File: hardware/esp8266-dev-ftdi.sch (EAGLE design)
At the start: 53 parts, among them CON1 USBMICRO-NO_CENTER-LONG_PADS

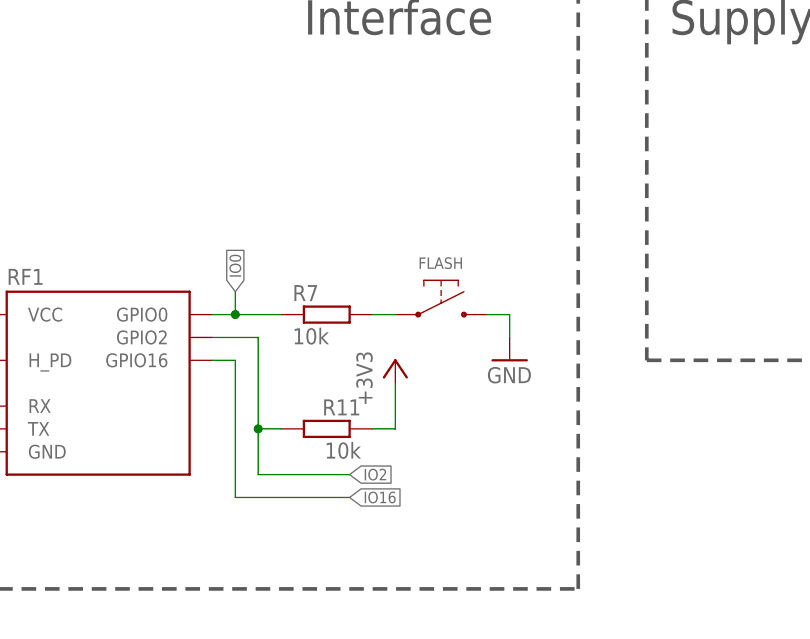
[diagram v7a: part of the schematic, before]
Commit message: added led to gpio2
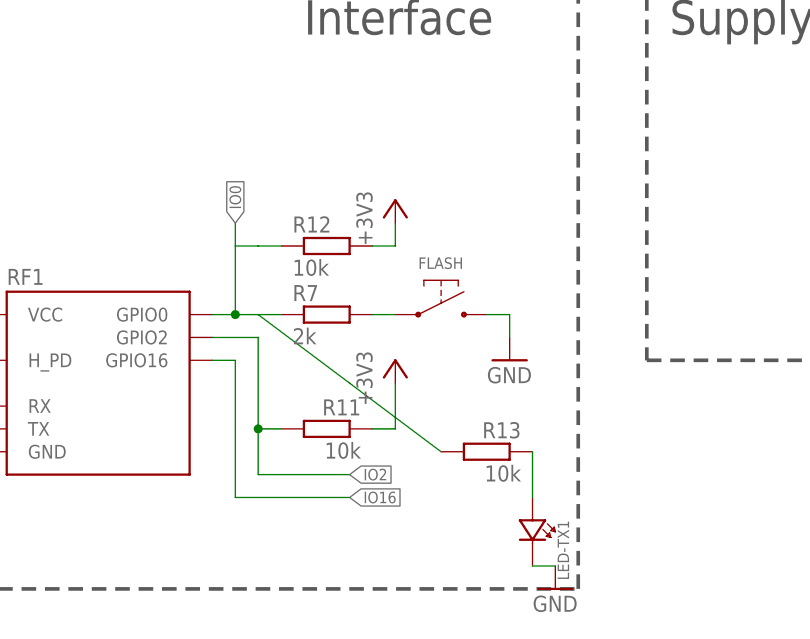
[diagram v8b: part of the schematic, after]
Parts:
- added LED-TX1: (no value), p.peter-leds:LED0805
- added R12, R13: 10k, p.peter-rcl:R-EU_R0805
- R7: value 10k -> 2k
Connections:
- new net N$22: LED-TX1.A, R13.1
- net +3V3: now also R12.2
- net GND: now also LED-TX1.C
- net IO0: now also R12.1, R13.2
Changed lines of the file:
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@@
 <?xml version="1.0" encoding="utf-8"?>
 <!DOCTYPE eagle SYSTEM "eagle.dtd">
-<eagle version="7.3.0">
+<eagle version="7.1.0">
 <drawing>
 <settings>
@@
 <part name="R6" library="p.peter-rcl" deviceset="R-EU_" device="R0805" value="10k"/>
 <part name="+3V8" library="supply1" deviceset="+3V3" device=""/>
-<part name="R7" library="p.peter-rcl" deviceset="R-EU_" device="R0805" value="10k"/>
+<part name="R7" library="p.peter-rcl" deviceset="R-EU_" device="R0805" value="2k"/>
 <part name="GND13" library="supply1" deviceset="GND" device=""/>
 <part name="U$2" library="p.peter-connectors" deviceset="UART-6_PIN" device="GENERIC"/>
@@
 <part name="3V3" library="testpad" deviceset="TPSQ" device="TP15R"/>
 <part name="GND" library="testpad" deviceset="TPSQ" device="TP15R"/>
+<part name="R12" library="p.peter-rcl" deviceset="R-EU_" device="R0805" value="10k"/>
+<part name="+3V9" library="supply1" deviceset="+3V3" device=""/>
+<part name="R13" library="p.peter-rcl" deviceset="R-EU_" device="R0805" value="10k"/>
+<part name="LED-TX1" library="p.peter-leds" deviceset="LED" device="0805"/>
+<part name="GND25" library="supply1" deviceset="GND" device=""/>
 </parts>
 <sheets>
@@
 <instance part="3V3" gate="G$1" x="73.66" y="71.12"/>
 <instance part="GND" gate="G$1" x="78.74" y="71.12"/>
+<instance part="R12" gate="G$1" x="106.68" y="-50.8"/>
+<instance part="+3V9" gate="G$1" x="114.3" y="-45.72"/>
+<instance part="R13" gate="G$1" x="124.46" y="-73.66" rot="MR0"/>
+<instance part="LED-TX1" gate="G$1" x="129.54" y="-81.28" rot="R270"/>
+<instance part="GND25" gate="1" x="132.08" y="-88.9"/>
 </instances>
 <busses>
@@
 <wire x1="78.74" y1="76.2" x2="78.74" y2="73.66" width="0.1524" layer="91"/>
 <pinref part="GND" gate="G$1" pin="TP"/>
+</segment>
+<segment>
+<pinref part="LED-TX1" gate="G$1" pin="C"/>
+<pinref part="GND25" gate="1" pin="GND"/>
+<wire x1="132.08" y1="-86.36" x2="129.54" y2="-86.36" width="0.1524" layer="91"/>
 </segment>
 </net>
@@
 <wire x1="73.66" y1="76.2" x2="73.66" y2="73.66" width="0.1524" layer="91"/>
 <pinref part="3V3" gate="G$1" pin="TP"/>
+</segment>
+<segment>
+<pinref part="R12" gate="G$1" pin="2"/>
+<pinref part="+3V9" gate="G$1" pin="+3V3"/>
+<wire x1="111.76" y1="-50.8" x2="114.3" y2="-50.8" width="0.1524" layer="91"/>
+<wire x1="114.3" y1="-50.8" x2="114.3" y2="-48.26" width="0.1524" layer="91"/>
 </segment>
 </net>
@@
 <pinref part="RF1" gate="G$1" pin="GPIO0"/>
 <pinref part="R7" gate="G$1" pin="1"/>
-<wire x1="101.6" y1="-58.42" x2="96.52" y2="-58.42" width="0.1524" layer="91"/>
+<wire x1="101.6" y1="-58.42" x2="99.06" y2="-58.42" width="0.1524" layer="91"/>
+<wire x1="99.06" y1="-58.42" x2="96.52" y2="-58.42" width="0.1524" layer="91"/>
 <wire x1="96.52" y1="-58.42" x2="93.98" y2="-58.42" width="0.1524" layer="91"/>
-<wire x1="96.52" y1="-58.42" x2="96.52" y2="-55.88" width="0.1524" layer="91"/>
+<wire x1="96.52" y1="-58.42" x2="96.52" y2="-50.8" width="0.1524" layer="91"/>
 <junction x="96.52" y="-58.42"/>
-<label x="96.52" y="-55.88" size="1.27" layer="95" rot="R90" xref="yes"/>
+<label x="96.52" y="-48.26" size="1.27" layer="95" rot="R90" xref="yes"/>
+<pinref part="R12" gate="G$1" pin="1"/>
+<wire x1="96.52" y1="-50.8" x2="96.52" y2="-48.26" width="0.1524" layer="91"/>
+<wire x1="101.6" y1="-50.8" x2="99.06" y2="-50.8" width="0.1524" layer="91"/>
+<wire x1="99.06" y1="-50.8" x2="96.52" y2="-50.8" width="0.1524" layer="91"/>
+<pinref part="R13" gate="G$1" pin="2"/>
+<wire x1="99.06" y1="-58.42" x2="109.22" y2="-66.04" width="0.1524" layer="91"/>
+<wire x1="109.22" y1="-66.04" x2="119.38" y2="-73.66" width="0.1524" layer="91"/>
 </segment>
 <segment>
@@
 </segment>
 </net>
+<net name="N$22" class="0">
+<segment>
+<pinref part="R13" gate="G$1" pin="1"/>
+<pinref part="LED-TX1" gate="G$1" pin="A"/>
+<wire x1="129.54" y1="-78.74" x2="129.54" y2="-73.66" width="0.1524" layer="91"/>
+</segment>
+</net>
